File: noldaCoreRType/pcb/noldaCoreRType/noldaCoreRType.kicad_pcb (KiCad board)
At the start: 2 copper layers, 68 x 76.5 mm, 79 parts, among them J1 Conn_01x10_Female, J2 USB_C_Receptacle_USB2.0, J3 Conn_01x02_Female, J4 Conn_01x06_Female, Q1 AO3401A, SW1 SW_Push, SW10 Choc, SW11 SW_Push, SW2 Choc, SW3 Choc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

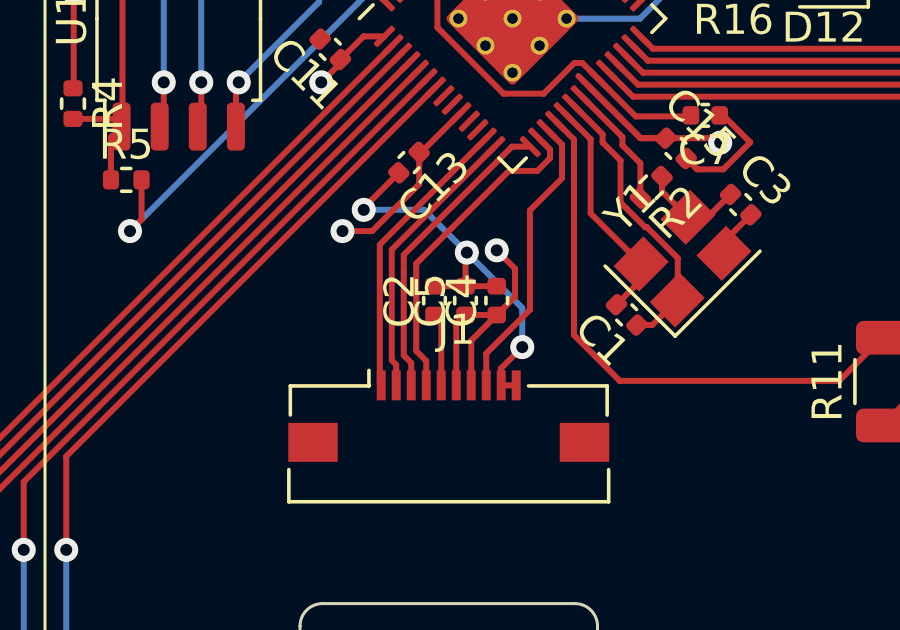
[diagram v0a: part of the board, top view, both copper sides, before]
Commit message: add u8g2
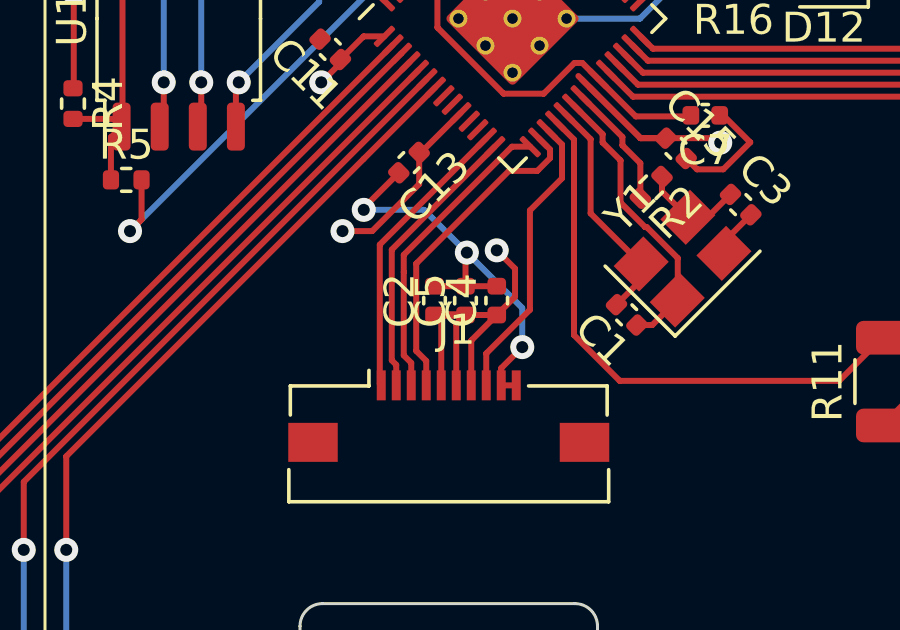
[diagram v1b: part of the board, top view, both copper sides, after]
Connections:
- C2 pad 1: SHARP_DISP -> +3V3
- J1 pad 5: SHARP_DISP -> +3V3
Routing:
- net +3V3: track 60.8 -> 64.3 mm
- net SHARP_DISP: track 2.44 -> 0.00 mm
